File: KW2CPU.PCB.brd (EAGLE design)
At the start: 50 x 30 mm, 50 parts, among them IC1 AT45DB161D8S1

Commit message: Working on layout
...4 layers is kind of annoying.
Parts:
- removed L$6, R$4, R$5: (no value), GW-devices:RF-L0201
- added C$6, L$4, L$5: (no value), GW-devices:RF-L0201
- added IC2: (no value), microchip:SOT223
- added R$1: (no value), GW-devices:RFMD0402
- added U$10, U$11, U$8, U$9: (no value), GW-devices:RF-R0402
- moved C$13 34.0 mm to (30.9, 0.07)
- moved C$15 34.0 mm to (30.9, -2.83)
- moved C$16 34.0 mm to (30.9, 5.11)
- moved C$18 34.0 mm to (30.8, 2.52)
- moved C$20 34.0 mm to (28.9, 5.57)
- moved C$21 34.0 mm to (27.1, 5.56)
- moved C$22 34.0 mm to (23.8, 5.90)
- moved C$24 34.0 mm to (22.9, 3.19)
- moved C1 34.0 mm to (22.1, 7.90)
- moved C10 34.0 mm to (8.60, -0.70)
- moved C11 34.0 mm to (8.60, -1.70)
- moved C12 34.0 mm to (8.60, -2.70)
- moved C16 34.0 mm to (20.5, -3.50)
- moved C17 34.0 mm to (20.5, -1.50)
- moved C18 34.0 mm to (20.5, -2.50)
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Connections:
- new net N$29: R$1.P$1, U$3.P$23
- new net N$51: IC1.4, U$8.1
- new net N$52: IC1.2, U$9.1
- new net N$53: IC1.1, U$10.1
- new net N$54: IC1.8, U$11.1
- new net VIN: IC2.3, U$6.P$38, U$6.P$40
- net +3V3: now also IC2.1, U$6.P$37, U$6.P$39
- net GND: now also IC2.2, IC2.4, R$1.P$2, U$4.P$3, U$4.P$4, U$6.P$1, U$6.P$2, U$6.P$3, U$6.P$4; no longer U$3.P$23
- net N$10: now also U$6.P$8; no longer U$6.P$4
- net N$11: now also U$6.P$10; no longer U$6.P$6
- net N$12: now also U$6.P$12; no longer U$6.P$8
- net N$13: now also U$6.P$14; no longer U$6.P$10
- net N$14: now also U$6.P$6; no longer U$6.P$2
- net N$15: now also U$6.P$16; no longer U$6.P$12
- net N$16: now also U$6.P$24, U$9.2; no longer IC1.2
- net N$17: now also U$10.2, U$6.P$26; no longer IC1.1
- net N$18: now also U$11.2, U$6.P$28; no longer IC1.8
- net N$2: now also L$5.P$1; no longer R$5.P$1
- net N$3: now also L$4.P$1; no longer R$4.P$1
- net N$33: now also U$6.P$7; no longer U$6.P$3
- net N$34: now also U$6.P$5; no longer U$6.P$1
- net N$35: now also U$6.P$9; no longer U$6.P$5
- net N$36: now also U$6.P$11; no longer U$6.P$7
- net N$37: now also U$6.P$13; no longer U$6.P$9
- net N$38: now also U$6.P$15; no longer U$6.P$11
- net N$39: now also U$6.P$17; no longer U$6.P$13
- net N$4: now also C$6.P$2, L$4.P$2; no longer L$6.P$2, R$4.P$2
- net N$40: now also U$6.P$19; no longer U$6.P$15
- net N$41: now also U$6.P$21; no longer U$6.P$17
- net N$42: now also U$6.P$23; no longer U$6.P$19
- net N$43: now also U$6.P$25; no longer U$6.P$21
- net N$44: now also U$6.P$27; no longer U$6.P$23
- net N$45: now also U$6.P$29; no longer U$6.P$25
- net N$46: now also U$6.P$31; no longer U$6.P$27
- net N$47: now also U$6.P$33; no longer U$6.P$29
- net N$48: now also U$6.P$35; no longer U$6.P$31
- net N$49: now also U$6.P$18; no longer U$6.P$14
- net N$5: now also C$6.P$1, L$5.P$2; no longer L$6.P$1, R$5.P$2
- net N$50: now also U$6.P$20; no longer U$6.P$16
- net N$7: now also U$6.P$22, U$8.2; no longer IC1.4
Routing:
- net +3V3: track 0.00 -> 40.3 mm, vias 0 -> 4
- net N$7: track 0.00 -> 34.2 mm, vias 0 -> 2
- net N$34: track 0.00 -> 29.3 mm
- net N$16: track 0.00 -> 28.7 mm, vias 0 -> 2
- net N$14: track 0.00 -> 27.4 mm, vias 0 -> 2
- net N$18: track 0.00 -> 26.8 mm, vias 0 -> 2
- net N$50: track 0.00 -> 26.7 mm, vias 0 -> 2
- net N$49: track 0.00 -> 26.3 mm, vias 0 -> 2
- net N$15: track 0.00 -> 26.1 mm, vias 0 -> 2
- net N$17: track 0.00 -> 26.0 mm, vias 0 -> 2
- net N$13: track 0.00 -> 25.4 mm, vias 0 -> 2
- net N$12: track 0.00 -> 24.9 mm, vias 0 -> 2
- net N$11: track 0.00 -> 24.2 mm, vias 0 -> 2
- net N$10: track 0.00 -> 23.5 mm, vias 0 -> 2
- net GND: track 3.17 -> 17.0 mm, vias 0 -> 29
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- added copper zone on layer 3, net +3V3
- added copper zone on layer 1, net GND
- added copper zone on layer 16, net GND
- added copper zone on layer 2, net GND

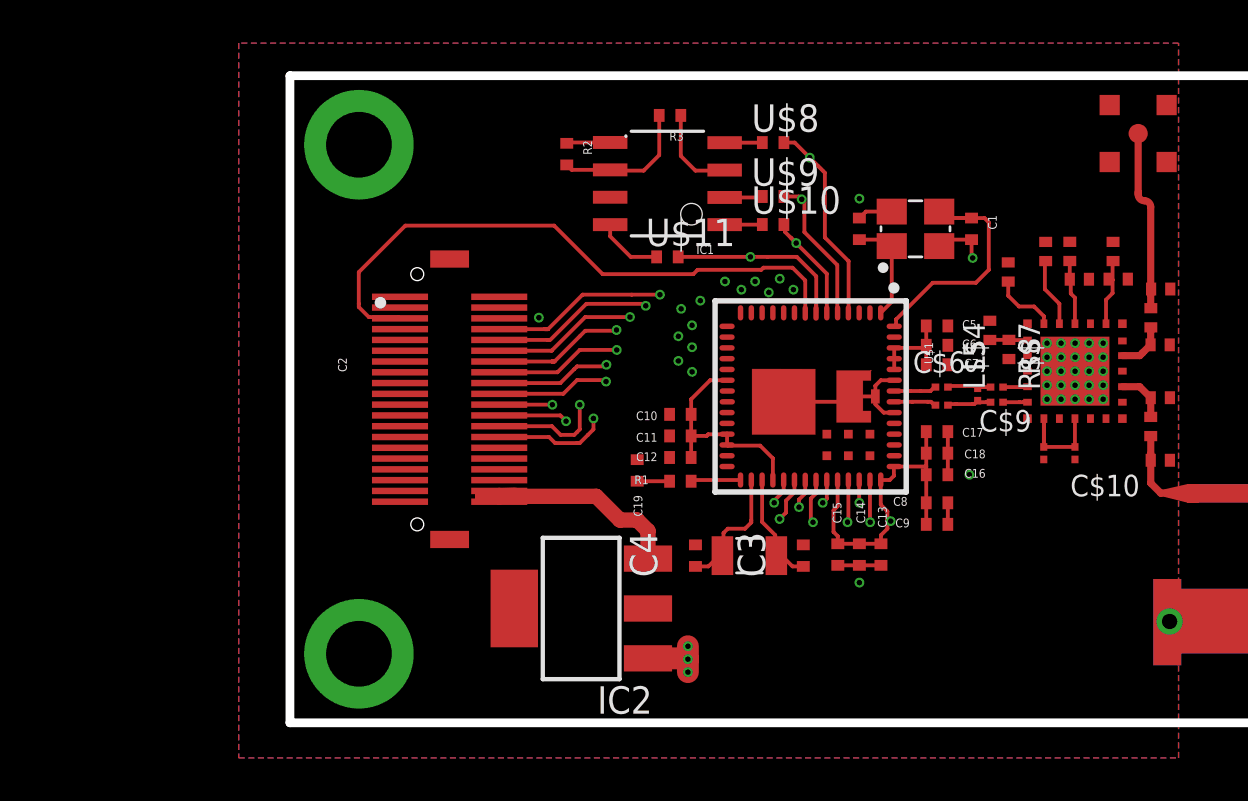
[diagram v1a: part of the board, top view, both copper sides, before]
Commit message: Added JTAG
Topside connector. Still needs routing
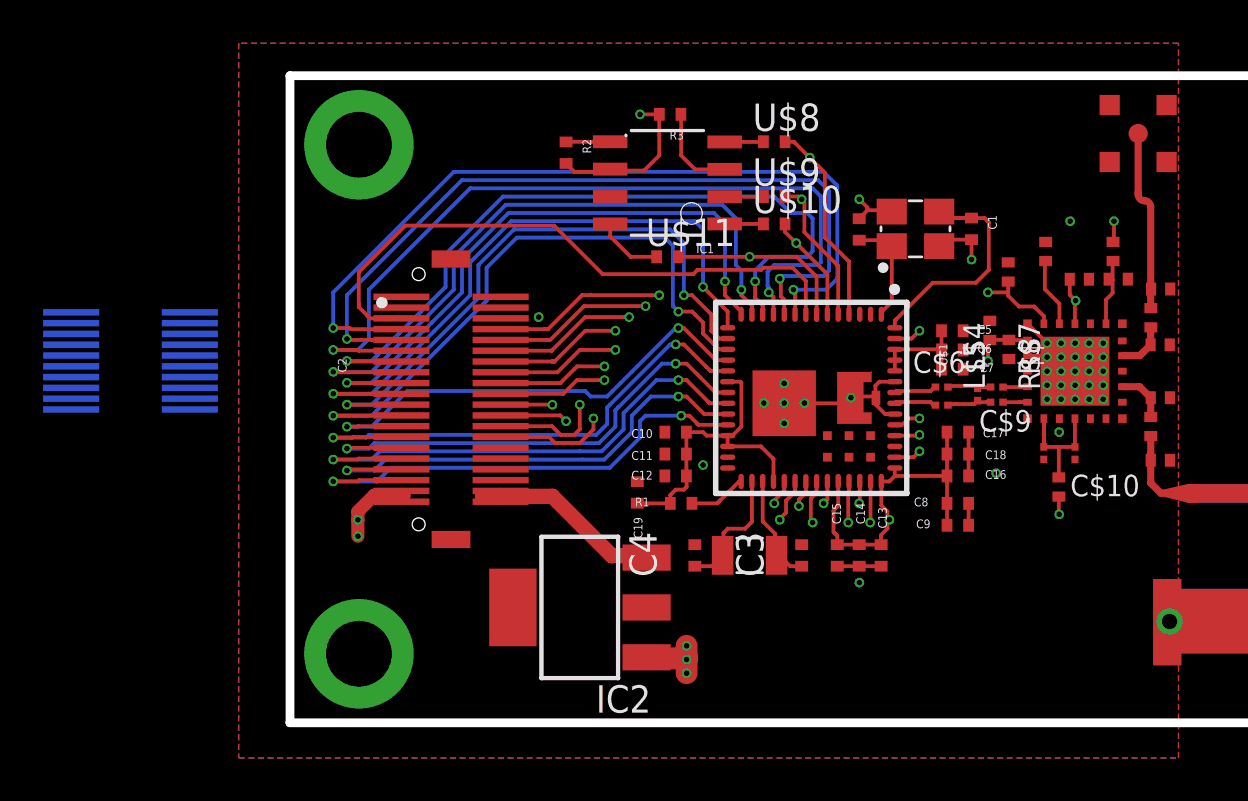
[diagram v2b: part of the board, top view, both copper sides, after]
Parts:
- added U$12: MOLEX55560-0207, KW2:MOLEX55560-0207
- moved L$11 10.9 mm to (26.1, -4.07)
- moved R1 1.03 mm to (8.64, -4.83)
- moved C19 1.02 mm to (6.60, -4.32)
- moved C16 0.96 mm to (21.5, -3.56)
- moved C9 0.96 mm to (21.5, -5.84)
- moved C18 0.96 mm to (21.5, -2.54)
- moved C8 0.96 mm to (21.5, -4.83)
- moved C17 0.96 mm to (21.5, -1.52)
- moved C12 0.88 mm to (8.38, -3.56)
- moved C11 0.87 mm to (8.38, -2.54)
- moved C10 0.85 mm to (8.38, -1.52)
- moved C5 0.74 mm to (21.2, 3.17)
- moved C6 0.74 mm to (21.2, 2.29)
- moved C7 0.74 mm to (21.2, 1.40)
- moved IC2 0.08 mm to (3.94, -9.65)
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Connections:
- net +3V3: now also U$12.P$2
- net GND: now also U$12.P$10, U$12.P$16, U$12.P$18, U$12.P$20, U$12.P$4, U$12.P$6
- net N$10: now also U$12.P$3
- net N$11: now also U$12.P$7
- net N$12: now also U$12.P$5
- net N$13: now also U$12.P$1
- net N$14: now also U$12.P$9
- net N$40: now also U$12.P$11
- net N$41: now also U$12.P$19
- net N$42: now also U$12.P$17
- net N$43: now also U$12.P$15
- net N$44: now also U$12.P$13
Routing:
- net N$33: track 0.00 -> 38.5 mm, vias 0 -> 2
- net N$36: track 0.00 -> 38.2 mm, vias 0 -> 2
- net N$35: track 0.00 -> 37.2 mm, vias 0 -> 2
- net N$37: track 0.00 -> 35.3 mm, vias 0 -> 2
- net N$22: track 5.38 -> 37.7 mm, vias 0 -> 1
- net N$38: track 0.00 -> 31.0 mm, vias 0 -> 2
- net N$42: track 0.00 -> 29.8 mm, vias 0 -> 2
- net N$40: track 0.00 -> 29.7 mm, vias 0 -> 2
- net N$39: track 0.00 -> 28.9 mm, vias 0 -> 2
- net N$41: track 0.00 -> 28.4 mm, vias 0 -> 2
- net N$26: track 0.00 -> 27.1 mm, vias 0 -> 2
- net N$44: track 0.00 -> 24.2 mm, vias 0 -> 2
- net N$46: track 0.00 -> 23.9 mm, vias 0 -> 2
- net N$48: track 0.00 -> 23.4 mm, vias 0 -> 2
- net N$43: track 0.00 -> 22.9 mm, vias 0 -> 2
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
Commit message: JTAG, RF Conn trace
Added JTAG connector, adjusted arcs on RF connector trace and added GND
vias
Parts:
- moved U$12 15.9 mm to (-1.02, 0.25), turned to 0 degrees
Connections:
- net +3V3: now also U$12.P$1; no longer U$12.P$2
- net GND: now also U$12.P$15, U$12.P$17, U$12.P$19, U$12.P$3, U$12.P$5, U$12.P$9; no longer U$12.P$10, U$12.P$16, U$12.P$18, U$12.P$20, U$12.P$4, U$12.P$6
- net N$10: now also U$12.P$4; no longer U$12.P$3
- net N$11: now also U$12.P$8; no longer U$12.P$7
- net N$12: now also U$12.P$6; no longer U$12.P$5
- net N$13: now also U$12.P$2; no longer U$12.P$1
- net N$14: now also U$12.P$10; no longer U$12.P$9
- net N$40: now also U$12.P$12; no longer U$12.P$11
- net N$41: now also U$12.P$20; no longer U$12.P$19
- net N$42: now also U$12.P$18; no longer U$12.P$17
- net N$43: now also U$12.P$16; no longer U$12.P$15
- net N$44: now also U$12.P$14; no longer U$12.P$13
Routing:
- net N$11: track 24.0 -> 40.0 mm
- net +3V3: track 50.4 -> 65.0 mm
- net N$12: track 24.8 -> 38.9 mm
- net N$10: track 23.3 -> 34.5 mm
- net N$44: track 24.2 -> 34.4 mm
- net N$14: track 27.3 -> 36.5 mm
- net N$43: track 22.9 -> 31.8 mm
- net N$42: track 29.8 -> 38.6 mm
- net N$40: track 29.7 -> 38.2 mm
- net N$13: track 25.2 -> 33.1 mm
- net N$41: track 28.4 -> 33.6 mm
- net GND: vias 37 -> 83
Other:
- board text added: "JTAG"
- board text added: "KW2CPU.v1.0"
